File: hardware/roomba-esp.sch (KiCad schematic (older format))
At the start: 7 parts, among them P1 CONN_01X07, P2 CONN_02X10, U1 ESP-12E, U2 LM2596_module

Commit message: initial version with unfinished pcb
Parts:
- D1: renamed from D?; footprint (none) -> LEDs:LED-0805
- P1: footprint (none) -> mini din:mini din 7
- P2: footprint (none) -> Socket_Strips:Socket_Strip_Straight_2x10
- R1: footprint (none) -> Resistors_SMD:R_0805_HandSoldering
- R2: renamed from R?; footprint (none) -> Resistors_SMD:R_0805_HandSoldering
- U1: footprint (none) -> ESP8266:ESP-12E
- U2: footprint (none) -> LM2596:LM2596_module
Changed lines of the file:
@@
 LIBS:contrib
 LIBS:valves
-LIBS:ESP8266
 LIBS:lm2596_module
 LIBS:roomba-esp-cache
@@
 F 0 "U1" H 5150 2500 50  0000 C CNN
 F 1 "ESP-12E" H 5150 2700 50  0000 C CNN
-F 2 "" H 5150 2600 50  0001 C CNN
+F 2 "ESP8266:ESP-12E" H 5150 2600 50  0001 C CNN
 F 3 "" H 5150 2600 50  0001 C CNN
 	1    5150 2600
-	1    0    0    -1
-$EndComp
-$Comp
-L LM2596_module U2
-U 1 1 55D5BA31
-P 9000 2700
-F 0 "U2" H 9000 2550 60  0000 C CNN
-F 1 "LM2596_module" H 9200 2800 60  0000 C CNN
-F 2 "" H 8100 2500 60  0000 C CNN
-F 3 "" H 8100 2500 60  0000 C CNN
-	1    9000 2700
-	1    0    0    -1
-$EndComp
-$Comp
-L CONN_01X07 P1
-U 1 1 55D5BABE
-P 8900 4050
-F 0 "P1" H 8900 4450 50  0000 C CNN
-F 1 "CONN_01X07" V 9000 4050 50  0000 C CNN
-F 2 "" H 8900 4050 60  0000 C CNN
-F 3 "" H 8900 4050 60  0000 C CNN
-	1    8900 4050
 	1    0    0    -1
 $EndComp
@@
 F 0 "R1" V 3480 2300 50  0000 C CNN
 F 1 "10K" V 3400 2300 50  0000 C CNN
-F 2 "" V 3330 2300 30  0000 C CNN
+F 2 "Resistors_SMD:R_0805_HandSoldering" V 3330 2300 30  0001 C CNN
 F 3 "" H 3400 2300 30  0000 C CNN
 	1    3400 2300
@@
 L GND #PWR03
 U 1 1 55D5BDC3
-P 9900 3100
-F 0 "#PWR03" H 9900 2850 50  0001 C CNN
-F 1 "GND" H 9900 2950 50  0000 C CNN
-F 2 "" H 9900 3100 60  0000 C CNN
-F 3 "" H 9900 3100 60  0000 C CNN
-	1    9900 3100
+P 9800 2900
+F 0 "#PWR03" H 9800 2650 50  0001 C CNN
+F 1 "GND" H 9800 2750 50  0000 C CNN
+F 2 "" H 9800 2900 60  0000 C CNN
+F 3 "" H 9800 2900 60  0000 C CNN
+	1    9800 2900
 	1    0    0    -1
 $EndComp
@@
 L GND #PWR04
 U 1 1 55D5BE37
-P 8150 3050
-F 0 "#PWR04" H 8150 2800 50  0001 C CNN
-F 1 "GND" H 8150 2900 50  0000 C CNN
-F 2 "" H 8150 3050 60  0000 C CNN
-F 3 "" H 8150 3050 60  0000 C CNN
-	1    8150 3050
+P 8200 2950
+F 0 "#PWR04" H 8200 2700 50  0001 C CNN
+F 1 "GND" H 8200 2800 50  0000 C CNN
+F 2 "" H 8200 2950 60  0000 C CNN
+F 3 "" H 8200 2950 60  0000 C CNN
+	1    8200 2950
 	1    0    0    -1
 $EndComp
@@
 L PWR_FLAG #FLG08
 U 1 1 55D5C164
-P 8150 2800
-F 0 "#FLG08" H 8150 2895 50  0001 C CNN
-F 1 "PWR_FLAG" H 8150 2980 50  0000 C CNN
-F 2 "" H 8150 2800 60  0000 C CNN
-F 3 "" H 8150 2800 60  0000 C CNN
-	1    8150 2800
+P 8200 2700
+F 0 "#FLG08" H 8200 2795 50  0001 C CNN
+F 1 "PWR_FLAG" H 8200 2880 50  0000 C CNN
+F 2 "" H 8200 2700 60  0000 C CNN
+F 3 "" H 8200 2700 60  0000 C CNN
+	1    8200 2700
 	1    0    0    -1
 $EndComp
@@
 	8150 2200 8150 2450
 Wire Wire Line
-	7800 2450 8250 2450
-Wire Wire Line
-	9950 2450 9750 2450
-Wire Wire Line
-	9900 2950 9900 3100
-Wire Wire Line
-	9900 2950 9750 2950
-Wire Wire Line
-	8150 2800 8150 3050
-Wire Wire Line
-	8150 2950 8250 2950
+	7800 2450 8350 2450
+Wire Wire Line
+	9650 2450 9950 2450
+Wire Wire Line
+	9800 2750 9800 2900
+Wire Wire Line
+	9800 2750 9650 2750
+Wire Wire Line
+	8200 2700 8200 2950
 Wire Wire Line
 	8450 4250 8450 4500
@@
 Wire Wire Line
 	3400 2850 3400 3000
-Connection ~ 8150 2950
 Wire Wire Line
 	7800 2150 7800 2450
@@
 F 0 "P2" H 6750 4800 50  0000 C CNN
 F 1 "CONN_02X10" V 6750 4250 50  0000 C CNN
-F 2 "" H 6750 3050 60  0000 C CNN
+F 2 "Socket_Strips:Socket_Strip_Straight_2x10" H 6750 3050 60  0001 C CNN
 F 3 "" H 6750 3050 60  0000 C CNN
 	1    6750 4250
@@
 Text Label 6200 4700 0    60   ~ 0
 GPIO14
-Text Label 7300 4700 0    60   ~ 0
-GPIO15
 Text Label 7300 4600 0    60   ~ 0
 GPIO16
@@
 GND
 $Comp
-L LED D?
+L LED D1
 U 1 1 55D5C706
 P 3100 2950
-F 0 "D?" H 3100 3050 50  0000 C CNN
+F 0 "D1" H 3100 3050 50  0000 C CNN
 F 1 "LED" H 3100 2850 50  0000 C CNN
-F 2 "" H 3100 2950 60  0000 C CNN
+F 2 "LEDs:LED-0805" H 3100 2950 60  0001 C CNN
 F 3 "" H 3100 2950 60  0000 C CNN
 	1    3100 2950
@@
 	3100 2600 3100 2750
 $Comp
-L R R?
+L R R2
 U 1 1 55D5C7B0
 P 3100 3450
-F 0 "R?" V 3180 3450 50  0000 C CNN
+F 0 "R2" V 3180 3450 50  0000 C CNN
 F 1 "1K" V 3100 3450 50  0000 C CNN
-F 2 "" V 3030 3450 30  0000 C CNN
+F 2 "Resistors_SMD:R_0805_HandSoldering" V 3030 3450 30  0001 C CNN
 F 3 "" H 3100 3450 30  0000 C CNN
 	1    3100 3450
@@
 	3100 3300 3100 3150
 $Comp
-L GND #PWR?
+L GND #PWR010
 U 1 1 55D5C835
 P 3100 3800
-F 0 "#PWR?" H 3100 3550 50  0001 C CNN
+F 0 "#PWR010" H 3100 3550 50  0001 C CNN
 F 1 "GND" H 3100 3650 50  0000 C CNN
 F 2 "" H 3100 3800 60  0000 C CNN
@@
 Wire Wire Line
 	3100 3800 3100 3600
+$Comp
+L LM2596_module U2
+U 1 1 56006BDB
+P 9000 2600
+F 0 "U2" H 9000 2650 60  0000 C CNN
+F 1 "LM2596_module" H 9000 2550 60  0000 C CNN
+F 2 "LM2596:LM2596_module" H 9000 2650 60  0001 C CNN
+F 3 "" H 9000 2650 60  0000 C CNN
+	1    9000 2600
+	1    0    0    -1
+$EndComp
+Wire Wire Line
+	8350 2750 8200 2750
+Connection ~ 8200 2750
+$Comp
+L CONN_01X07 P1
+U 1 1 560084A0
+P 8900 4050
+F 0 "P1" H 8900 4450 50  0000 C CNN
+F 1 "CONN_01X07" V 9000 4050 50  0000 C CNN
+F 2 "mini din:mini din 7" H 8900 4050 60  0001 C CNN
+F 3 "" H 8900 4050 60  0000 C CNN
+	1    8900 4050
+	1    0    0    -1
+$EndComp
+Text Label 7300 4700 0    60   ~ 0
+GPIO15
 $EndSCHEMATC

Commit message: finalised rev0 pcb
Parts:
- P1: footprint mini din:mini din 7 -> mini din:mini_DIN_7
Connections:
- net ADC: now also P2.19 (P19); no longer P2.6 (P6)
- net CS0: now also P2.12 (P12); no longer P2.16 (P16)
- net GPIO14: now also P2.18 (P18); no longer P2.19 (P19)
- net GPIO15: now also P2.16 (P16); no longer P2.20 (P20)
- net GPIO16: now also P2.14 (P14); no longer P2.18 (P18)
- net MISO: now also P2.10 (P10); no longer P2.14 (P14)
- net MOSI: now also P2.8 (P8); no longer P2.12 (P12)
- net RESET: now also P2.20 (P20); no longer P2.8 (P8)
- net SCK: now also P2.6 (P6); no longer P2.10 (P10)
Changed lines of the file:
@@
 LIBS:contrib
 LIBS:valves
-LIBS:lm2596_module
-LIBS:roomba-esp-cache
 EELAYER 25 0
 EELAYER END
@@
 Text Label 6200 4600 0    60   ~ 0
 GPIO13
+Text Label 7300 4600 0    60   ~ 0
+GPIO14
+Text Label 7300 4400 0    60   ~ 0
+GPIO16
+Text Label 7300 4300 0    60   ~ 0
+CS0
+Text Label 7300 4200 0    60   ~ 0
+MISO
+Text Label 7300 4100 0    60   ~ 0
+MOSI
+Text Label 7300 4000 0    60   ~ 0
+SCK
+Text Label 7300 4700 0    60   ~ 0
+RESET
 Text Label 6200 4700 0    60   ~ 0
-GPIO14
-Text Label 7300 4600 0    60   ~ 0
-GPIO16
-Text Label 7300 4500 0    60   ~ 0
-CS0
-Text Label 7300 4400 0    60   ~ 0
-MISO
-Text Label 7300 4300 0    60   ~ 0
-MOSI
-Text Label 7300 4200 0    60   ~ 0
-SCK
-Text Label 7300 4100 0    60   ~ 0
-RESET
-Text Label 7300 4000 0    60   ~ 0
 ADC
 Text Label 7300 3900 0    60   ~ 0
@@
 F 0 "P1" H 8900 4450 50  0000 C CNN
 F 1 "CONN_01X07" V 9000 4050 50  0000 C CNN
-F 2 "mini din:mini din 7" H 8900 4050 60  0001 C CNN
+F 2 "mini din:mini_DIN_7" H 8900 4050 60  0001 C CNN
 F 3 "" H 8900 4050 60  0000 C CNN
 	1    8900 4050
 	1    0    0    -1
 $EndComp
-Text Label 7300 4700 0    60   ~ 0
+Text Label 7300 4500 0    60   ~ 0
 GPIO15
 $EndSCHEMATC

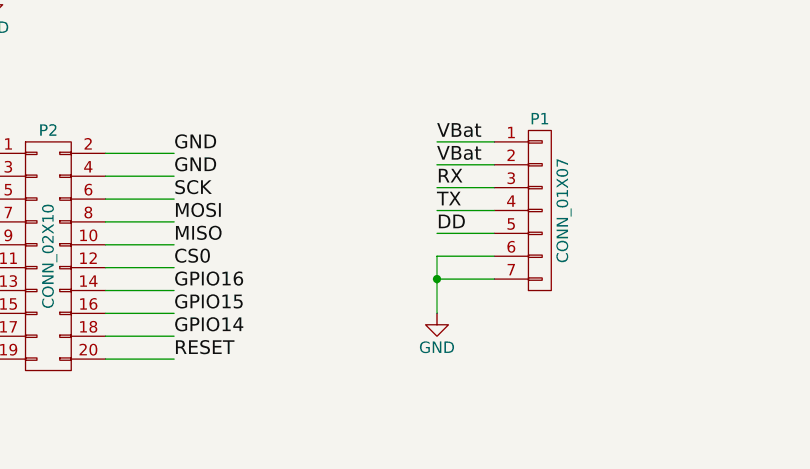
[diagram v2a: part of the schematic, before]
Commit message: added voltage divider on ESP RX to accomodate for 5V level on 3.3V pin
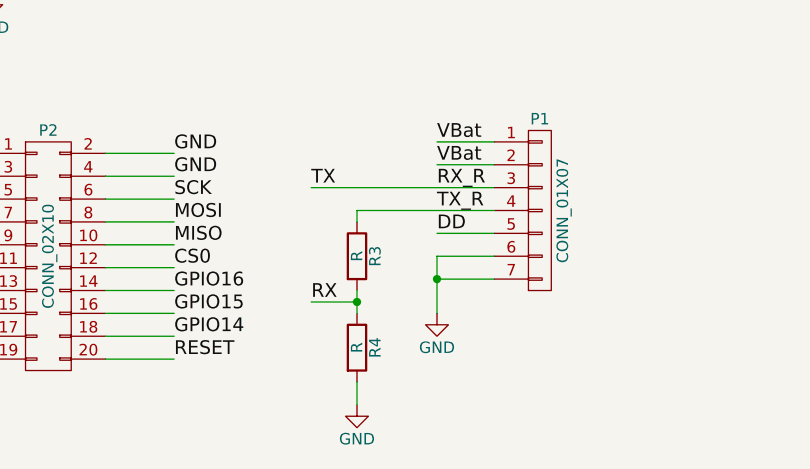
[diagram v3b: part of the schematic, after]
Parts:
- added R3, R4: R, Resistors_SMD:R_0805_HandSoldering, symbol R
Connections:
- net GND: now also R4.2
- net RX: now also R3.2, R4.1; no longer P1.3 (P3)
- net TX renamed RX_R
- net RX_R: now also P1.3 (P3); no longer P1.4 (P4)
- new net TX_R: P1.4 (P4), R3.1
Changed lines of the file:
@@
 LIBS:contrib
 LIBS:valves
+LIBS:lm2596_module
+LIBS:ESP8266
 EELAYER 25 0
 EELAYER END
@@
 VBat
 Text Label 8450 3950 0    60   ~ 0
-RX
+RX_R
 Text Label 8450 4050 0    60   ~ 0
-TX
+TX_R
 Text Label 8450 4150 0    60   ~ 0
 DD
@@
 	8700 3850 8450 3850
 Wire Wire Line
-	8700 3950 8450 3950
-Wire Wire Line
-	8700 4050 8450 4050
+	7900 3950 8700 3950
+Wire Wire Line
+	8100 4050 8700 4050
 Wire Wire Line
 	8700 4150 8450 4150
@@
 Text Label 7300 4500 0    60   ~ 0
 GPIO15
+$Comp
+L R R3
+U 1 1 5606DDFD
+P 8100 4250
+F 0 "R3" V 8180 4250 50  0000 C CNN
+F 1 "R" V 8100 4250 50  0000 C CNN
+F 2 "Resistors_SMD:R_0805_HandSoldering" V 8030 4250 30  0001 C CNN
+F 3 "" H 8100 4250 30  0000 C CNN
+	1    8100 4250
+	1    0    0    -1
+$EndComp
+$Comp
+L R R4
+U 1 1 5606DE8E
+P 8100 4650
+F 0 "R4" V 8180 4650 50  0000 C CNN
+F 1 "R" V 8100 4650 50  0000 C CNN
+F 2 "Resistors_SMD:R_0805_HandSoldering" V 8030 4650 30  0001 C CNN
+F 3 "" H 8100 4650 30  0000 C CNN
+	1    8100 4650
+	1    0    0    -1
+$EndComp
+Wire Wire Line
+	8100 4050 8100 4100
+$Comp
+L GND #PWR011
+U 1 1 5606DFE7
+P 8100 4900
+F 0 "#PWR011" H 8100 4650 50  0001 C CNN
+F 1 "GND" H 8100 4750 50  0000 C CNN
+F 2 "" H 8100 4900 60  0000 C CNN
+F 3 "" H 8100 4900 60  0000 C CNN
+	1    8100 4900
+	1    0    0    -1
+$EndComp
+Wire Wire Line
+	8100 4800 8100 4900
+Wire Wire Line
+	7900 4450 8100 4450
+Wire Wire Line
+	8100 4400 8100 4500
+Connection ~ 8100 4450
+Text Label 7900 4450 0    60   ~ 0
+RX
+Text Label 7900 3950 0    60   ~ 0
+TX
 $EndSCHEMATC

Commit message: added additional connector to serial in schematic
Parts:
- added P3: CONN_01X04, Socket_Strips:Socket_Strip_Straight_1x04, symbol CONN_01X04
- P2: footprint Socket_Strips:Socket_Strip_Straight_2x10 -> Socket_Strips:Socket_Strip_Angled_2x10
- R3: value R -> 5K
- R4: value R -> 10K
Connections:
- wire segments 69 -> 73
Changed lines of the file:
@@
 LIBS:lm2596_module
 LIBS:ESP8266
+LIBS:roomba-esp-cache
 EELAYER 25 0
 EELAYER END
@@
 F 0 "P2" H 6750 4800 50  0000 C CNN
 F 1 "CONN_02X10" V 6750 4250 50  0000 C CNN
-F 2 "Socket_Strips:Socket_Strip_Straight_2x10" H 6750 3050 60  0001 C CNN
+F 2 "Socket_Strips:Socket_Strip_Angled_2x10" H 6750 3050 60  0001 C CNN
 F 3 "" H 6750 3050 60  0000 C CNN
 	1    6750 4250
@@
 P 8100 4250
 F 0 "R3" V 8180 4250 50  0000 C CNN
-F 1 "R" V 8100 4250 50  0000 C CNN
+F 1 "5K" V 8100 4250 50  0000 C CNN
 F 2 "Resistors_SMD:R_0805_HandSoldering" V 8030 4250 30  0001 C CNN
 F 3 "" H 8100 4250 30  0000 C CNN
@@
 P 8100 4650
 F 0 "R4" V 8180 4650 50  0000 C CNN
-F 1 "R" V 8100 4650 50  0000 C CNN
+F 1 "10K" V 8100 4650 50  0000 C CNN
 F 2 "Resistors_SMD:R_0805_HandSoldering" V 8030 4650 30  0001 C CNN
 F 3 "" H 8100 4650 30  0000 C CNN
@@
 Text Label 7900 3950 0    60   ~ 0
 TX
+$Comp
+L CONN_01X04 P3
+U 1 1 56085904
+P 4300 5700
+F 0 "P3" H 4300 5950 50  0000 C CNN
+F 1 "CONN_01X04" V 4400 5700 50  0000 C CNN
+F 2 "Socket_Strips:Socket_Strip_Straight_1x04" H 4300 5700 60  0001 C CNN
+F 3 "" H 4300 5700 60  0000 C CNN
+	1    4300 5700
+	1    0    0    -1
+$EndComp
+Wire Wire Line
+	4100 5550 3800 5550
+Wire Wire Line
+	4100 5650 3800 5650
+Wire Wire Line
+	4100 5850 3800 5850
+Wire Wire Line
+	4100 5750 3800 5750
+Text Label 3800 5550 0    60   ~ 0
+VBat
+Text Label 3800 5850 0    60   ~ 0
+TX_R
+Text Label 3800 5750 0    60   ~ 0
+RX_R
+Text Label 3800 5650 0    60   ~ 0
+GND
 $EndSCHEMATC
